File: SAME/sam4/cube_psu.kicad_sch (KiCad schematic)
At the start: 19 parts, among them U4 i3A4W005A150V, U5 Cube_PSM, U6 i3A4W005A150V

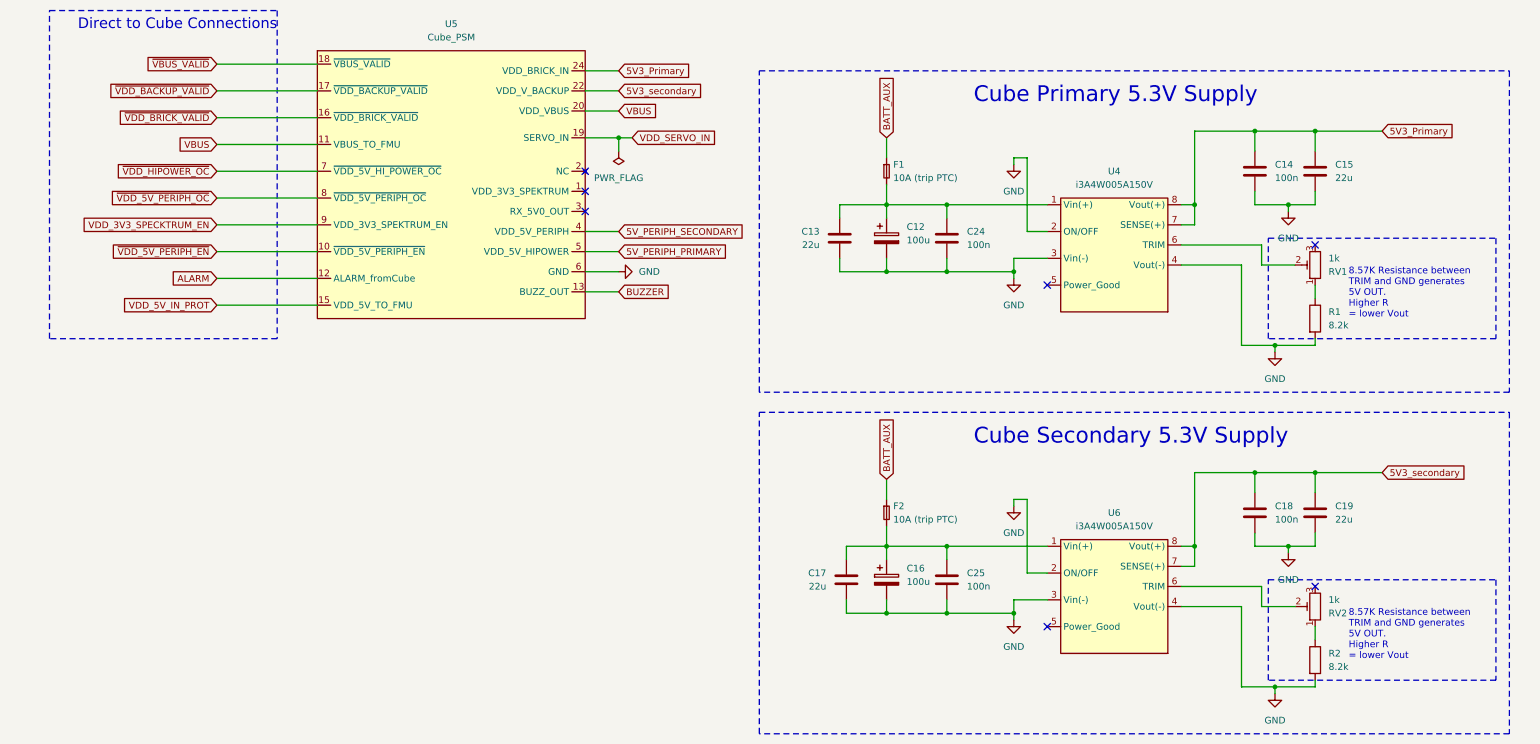
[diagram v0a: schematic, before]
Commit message: final san check routing. add protection
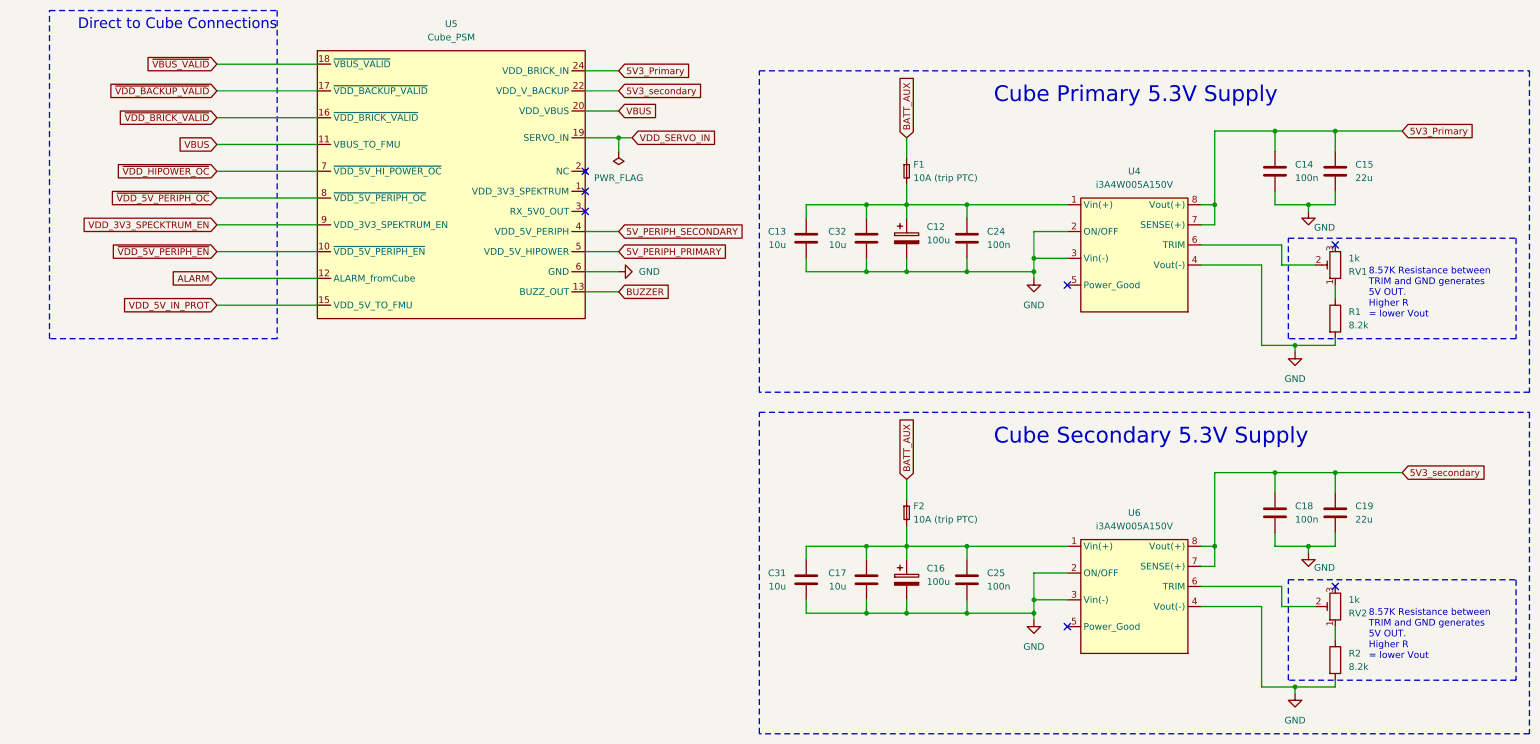
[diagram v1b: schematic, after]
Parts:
- added C31, C32: 10u, Capacitor_SMD:C_1206_3216Metric, symbol Device:C
- C13, C17: value 22u -> 10u; LCSC C12891 -> C13585
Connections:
- net GND: now also C31.2, C32.2
- net at C16.1, C17.1, C25.1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: now also C31.1
- net at C12.1, C13.1, C24.1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: now also C32.1
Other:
- moved on the sheet: C12, C14, C15, C16, C17, C18, C19, C24, C25, F1, F2, R1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

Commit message: add JLC ordering files. small tweaks
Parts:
- C12, C16: LCSC (none) -> C249588
- RV1, RV2: LCSC (none) -> C780233
- U4, U6: LCSC (none) -> C6061252
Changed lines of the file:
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@@
 			)
 		)
-		(property "Datasheet" ""
+		(property "Datasheet" "https://www.digikey.com/en/products/detail/tdk-lambda/I3A4W005A150V-001-R/7321112"
 			(at 223.52 113.03 0)
 			(effects
@@
 			)
 		)
-		(property "LCSC" ""
+		(property "LCSC" "C6061252"
 			(at 223.52 113.03 0)
 			(effects
@@
 			)
 		)
-		(property "LCSC" ""
+		(property "LCSC" "C249588"
 			(at 180.34 59.69 0)
 			(effects
@@
 			)
 		)
-		(property "LCSC" ""
+		(property "LCSC" "C249588"
 			(at 180.34 124.46 0)
 			(effects
@@
 			)
 		)
-		(property "LCSC" ""
+		(property "LCSC" "C780233"
 			(at 261.62 64.77 0)
 			(effects
@@
 			)
 		)
-		(property "LCSC" ""
+		(property "LCSC" "C780233"
 			(at 261.62 129.54 0)
 			(effects
@@
 			)
 		)
-		(property "Datasheet" ""
+		(property "Datasheet" "https://www.digikey.com/en/products/detail/tdk-lambda/I3A4W005A150V-001-R/7321112"
 			(at 223.52 48.26 0)
 			(effects
@@
 			)
 		)
-		(property "LCSC" ""
+		(property "LCSC" "C6061252"
 			(at 223.52 48.26 0)
 			(effects
